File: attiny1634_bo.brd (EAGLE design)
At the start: 49.5 x 22.2 mm, 11 parts, among them J1 AVR_SPI_PRG_6NS, Y1 12MHz

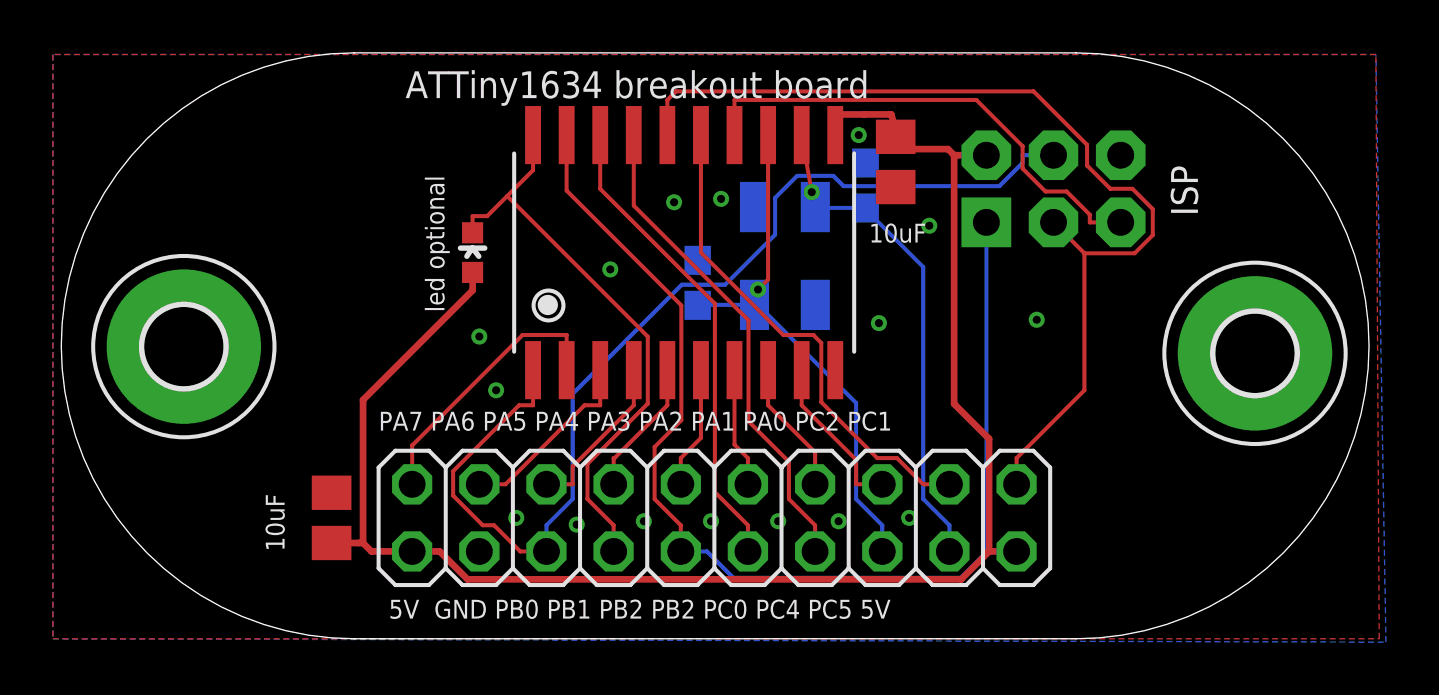
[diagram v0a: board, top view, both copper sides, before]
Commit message: small adjustment for better isolation
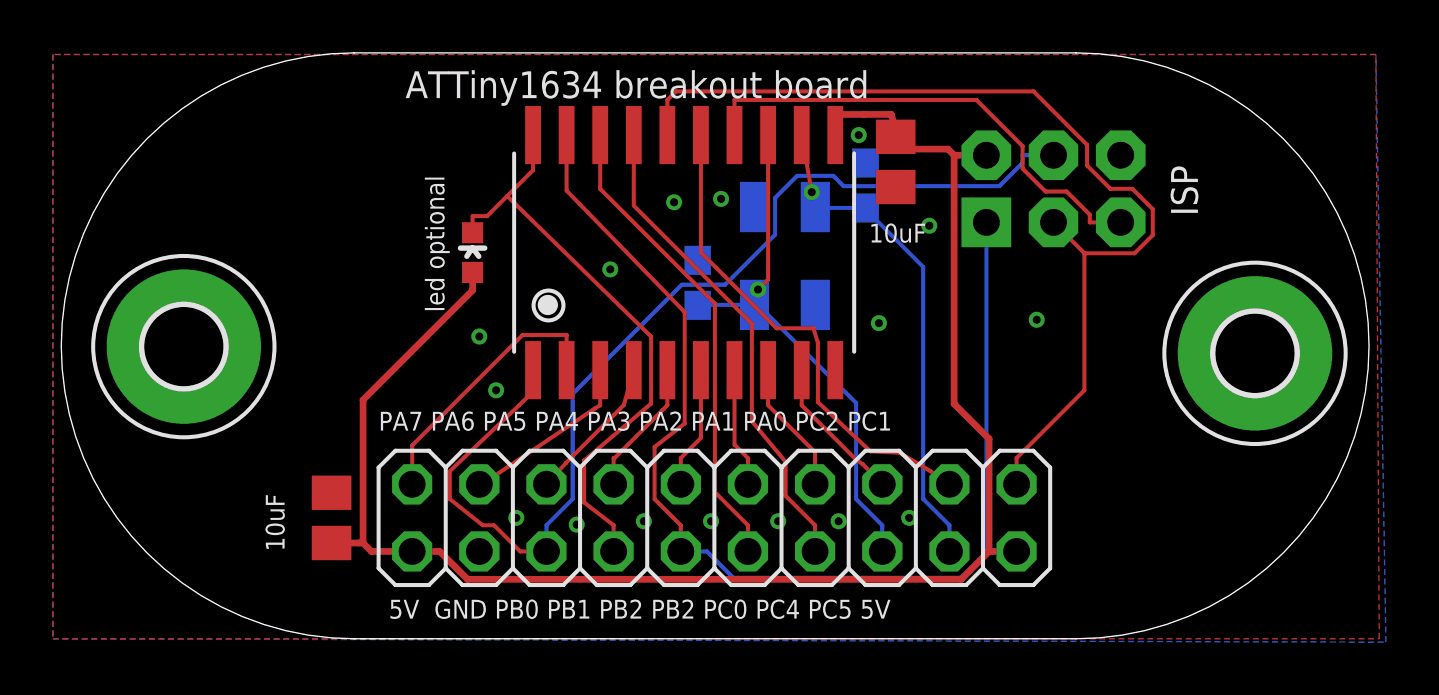
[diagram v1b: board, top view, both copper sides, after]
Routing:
- net PA5: track 6.27 -> 5.56 mm
- net PA0: track 6.16 -> 5.60 mm
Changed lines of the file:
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@@
 <wire x1="16.4234" y1="15.9837" x2="15.875" y2="15.9837" width="0.1524" layer="1"/>
 <wire x1="18.161" y1="17.7213" x2="17.1836" y2="16.7439" width="0.1524" layer="1"/>
-<wire x1="17.1836" y1="16.7439" x2="22.4998" y2="11.4277" width="0.1524" layer="1"/>
-<wire x1="22.4998" y1="11.4277" x2="22.4998" y2="8.8944" width="0.1524" layer="1"/>
-<wire x1="22.4998" y1="8.8944" x2="20.2183" y2="6.6129" width="0.1524" layer="1"/>
-<wire x1="20.2183" y1="6.6129" x2="20.2183" y2="5.2834" width="0.1524" layer="1"/>
-<wire x1="20.2183" y1="5.2834" x2="21.209" y2="4.2927" width="0.1524" layer="1"/>
+<wire x1="17.1836" y1="16.7439" x2="22.6268" y2="11.4277" width="0.1524" layer="1"/>
+<wire x1="22.6268" y1="11.4277" x2="22.6268" y2="8.8944" width="0.1524" layer="1"/>
+<wire x1="22.6268" y1="8.8944" x2="20.0913" y2="6.7399" width="0.1524" layer="1"/>
+<wire x1="20.0913" y1="6.7399" x2="20.0913" y2="5.1564" width="0.1524" layer="1"/>
+<wire x1="20.0913" y1="5.1564" x2="21.209" y2="4.2927" width="0.1524" layer="1"/>
 <wire x1="21.209" y1="3.302" x2="21.209" y2="4.2927" width="0.1524" layer="1"/>
 <wire x1="15.875" y1="15.355" x2="15.875" y2="15.9837" width="0.1524" layer="1"/>
@@
 <contactref element="JP1" pad="16"/>
 <wire x1="18.669" y1="3.302" x2="17.6783" y2="3.302" width="0.1524" layer="1"/>
-<wire x1="18.161" y1="10.16" x2="18.161" y2="8.8313" width="0.1524" layer="1"/>
-<wire x1="18.161" y1="8.8313" x2="17.6323" y2="8.8313" width="0.1524" layer="1"/>
-<wire x1="17.6323" y1="8.8313" x2="15.1382" y2="6.3372" width="0.1524" layer="1"/>
-<wire x1="15.1382" y1="6.3372" x2="15.1382" y2="5.4134" width="0.1524" layer="1"/>
-<wire x1="15.1382" y1="5.4134" x2="16.2589" y2="4.2927" width="0.1524" layer="1"/>
+<wire x1="18.161" y1="10.16" x2="18.161" y2="9.3393" width="0.1524" layer="1"/>
+<wire x1="18.161" y1="9.3393" x2="17.6323" y2="8.8313" width="0.1524" layer="1"/>
+<wire x1="17.6323" y1="8.8313" x2="15.0112" y2="6.3372" width="0.1524" layer="1"/>
+<wire x1="15.0112" y1="6.3372" x2="15.0112" y2="5.2864" width="0.1524" layer="1"/>
+<wire x1="15.0112" y1="5.2864" x2="16.2589" y2="4.2927" width="0.1524" layer="1"/>
 <wire x1="16.2589" y1="4.2927" x2="16.6876" y2="4.2927" width="0.1524" layer="1"/>
 <wire x1="16.6876" y1="4.2927" x2="17.6783" y2="3.302" width="0.1524" layer="1"/>
@@
 <wire x1="23.749" y1="3.302" x2="23.749" y2="4.2927" width="0.1524" layer="1"/>
 <wire x1="19.431" y1="19.05" x2="19.431" y2="16.9479" width="0.1524" layer="1"/>
-<wire x1="19.431" y1="16.9479" x2="23.7698" y2="12.6091" width="0.1524" layer="1"/>
-<wire x1="23.7698" y1="12.6091" x2="23.7698" y2="8.2657" width="0.1524" layer="1"/>
-<wire x1="23.7698" y1="8.2657" x2="22.7583" y2="7.2542" width="0.1524" layer="1"/>
+<wire x1="19.431" y1="16.9479" x2="23.8968" y2="12.3551" width="0.1524" layer="1"/>
+<wire x1="23.8968" y1="12.3551" x2="23.8968" y2="8.1387" width="0.1524" layer="1"/>
+<wire x1="23.8968" y1="8.1387" x2="22.7583" y2="7.2542" width="0.1524" layer="1"/>
 <wire x1="22.7583" y1="7.2542" x2="22.7583" y2="5.2834" width="0.1524" layer="1"/>
 <wire x1="22.7583" y1="5.2834" x2="23.749" y2="4.2927" width="0.1524" layer="1"/>
@@
 <contactref element="U$1" pad="9"/>
 <contactref element="JP1" pad="5"/>
-<wire x1="31.369" y1="5.842" x2="30.3783" y2="5.842" width="0.1524" layer="1"/>
+<wire x1="31.369" y1="5.842" x2="30.6323" y2="6.604" width="0.1524" layer="1"/>
 <wire x1="28.321" y1="10.16" x2="28.321" y2="8.8313" width="0.1524" layer="1"/>
 <wire x1="28.321" y1="8.8313" x2="30.3783" y2="6.774" width="0.1524" layer="1"/>
-<wire x1="30.3783" y1="6.774" x2="30.3783" y2="5.842" width="0.1524" layer="1"/>
+<wire x1="30.3783" y1="6.774" x2="30.6323" y2="6.604" width="0.1524" layer="1"/>
 </signal>
 <signal name="PA1">
@@
 <contactref element="JP1" pad="15"/>
 <contactref element="U$1" pad="4"/>
-<wire x1="18.669" y1="5.842" x2="19.6597" y2="5.842" width="0.1524" layer="1"/>
-<wire x1="21.971" y1="10.16" x2="21.971" y2="8.8313" width="0.1524" layer="1"/>
-<wire x1="21.971" y1="8.8313" x2="19.6597" y2="6.52" width="0.1524" layer="1"/>
-<wire x1="19.6597" y1="6.52" x2="19.6597" y2="5.842" width="0.1524" layer="1"/>
+<wire x1="18.669" y1="5.842" x2="18.8977" y2="6.096" width="0.1524" layer="1"/>
+<wire x1="21.971" y1="10.16" x2="21.59" y2="8.8313" width="0.1524" layer="1"/>
+<wire x1="21.59" y1="8.8313" x2="19.4057" y2="6.647" width="0.1524" layer="1"/>
+<wire x1="19.4057" y1="6.647" x2="18.8977" y2="6.096" width="0.1524" layer="1"/>
 </signal>
 <signal name="PA4">
@@
 <contactref element="JP1" pad="17"/>
 <contactref element="U$1" pad="3"/>
-<wire x1="16.129" y1="5.842" x2="17.1197" y2="5.842" width="0.1524" layer="1"/>
+<wire x1="16.129" y1="5.842" x2="16.6117" y2="6.096" width="0.1524" layer="1"/>
 <wire x1="20.701" y1="10.16" x2="20.701" y2="8.8313" width="0.1524" layer="1"/>
-<wire x1="20.701" y1="8.8313" x2="20.109" y2="8.8313" width="0.1524" layer="1"/>
-<wire x1="20.109" y1="8.8313" x2="17.1197" y2="5.842" width="0.1524" layer="1"/>
+<wire x1="20.701" y1="8.8313" x2="20.49" y2="8.7043" width="0.1524" layer="1"/>
+<wire x1="20.49" y1="8.7043" x2="16.6117" y2="6.096" width="0.1524" layer="1"/>
 </signal>
 <signal name="PB3/ADC8/OC1A">
@@
 <wire x1="28.829" y1="3.302" x2="28.829" y2="4.2927" width="0.1524" layer="1"/>
 <wire x1="21.971" y1="19.05" x2="21.971" y2="16.3787" width="0.1524" layer="1"/>
-<wire x1="21.971" y1="16.3787" x2="26.3098" y2="12.0399" width="0.1524" layer="1"/>
-<wire x1="26.3098" y1="12.0399" x2="26.3098" y2="8.2241" width="0.1524" layer="1"/>
-<wire x1="26.3098" y1="8.2241" x2="27.8383" y2="6.6956" width="0.1524" layer="1"/>
-<wire x1="27.8383" y1="6.6956" x2="27.8383" y2="5.2834" width="0.1524" layer="1"/>
-<wire x1="27.8383" y1="5.2834" x2="28.829" y2="4.2927" width="0.1524" layer="1"/>
+<wire x1="21.971" y1="16.3787" x2="26.4368" y2="11.9129" width="0.1524" layer="1"/>
+<wire x1="26.4368" y1="11.9129" x2="26.4368" y2="8.2241" width="0.1524" layer="1"/>
+<wire x1="26.4368" y1="8.2241" x2="27.7113" y2="6.6956" width="0.1524" layer="1"/>
+<wire x1="27.7113" y1="6.6956" x2="27.7113" y2="5.4104" width="0.1524" layer="1"/>
+<wire x1="27.7113" y1="5.4104" x2="28.829" y2="4.2927" width="0.1524" layer="1"/>
 </signal>
 <signal name="PC2/ADC11">
 <contactref element="U$1" pad="15"/>
 <contactref element="JP1" pad="3"/>
-<wire x1="33.909" y1="5.842" x2="32.9183" y2="5.842" width="0.1524" layer="1"/>
-<wire x1="32.9183" y1="5.842" x2="31.9276" y2="6.8327" width="0.1524" layer="1"/>
-<wire x1="31.9276" y1="6.8327" x2="31.1789" y2="6.8327" width="0.1524" layer="1"/>
-<wire x1="31.1789" y1="6.8327" x2="29.0622" y2="8.9494" width="0.1524" layer="1"/>
-<wire x1="29.0622" y1="8.9494" x2="29.0622" y2="11.1904" width="0.1524" layer="1"/>
-<wire x1="29.0622" y1="11.1904" x2="28.7638" y2="11.4888" width="0.1524" layer="1"/>
-<wire x1="28.7638" y1="11.4888" x2="27.6274" y2="11.4888" width="0.1524" layer="1"/>
-<wire x1="27.6274" y1="11.4888" x2="24.511" y2="14.6052" width="0.1524" layer="1"/>
+<wire x1="33.909" y1="5.842" x2="33.1723" y2="6.35" width="0.1524" layer="1"/>
+<wire x1="33.1723" y1="6.35" x2="32.0293" y2="7.0356" width="0.1524" layer="1"/>
+<wire x1="32.0293" y1="7.0356" x2="30.9249" y2="7.0867" width="0.1524" layer="1"/>
+<wire x1="30.9249" y1="7.0867" x2="28.9352" y2="8.9494" width="0.1524" layer="1"/>
+<wire x1="28.9352" y1="8.9494" x2="28.9352" y2="11.1904" width="0.1524" layer="1"/>
+<wire x1="28.9352" y1="11.1904" x2="28.7638" y2="11.7428" width="0.1524" layer="1"/>
+<wire x1="28.7638" y1="11.7428" x2="27.3734" y2="11.7428" width="0.1524" layer="1"/>
+<wire x1="27.3734" y1="11.7428" x2="24.511" y2="14.6052" width="0.1524" layer="1"/>
 <wire x1="24.511" y1="14.6052" x2="24.511" y2="19.05" width="0.1524" layer="1"/>
 </signal>

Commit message: I think it is now good enough
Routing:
- net PC1/SCL/ADC10: track 37.4 -> 38.1 mm
- net +5V: track 62.5 -> 63.2 mm
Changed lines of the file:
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@@
 <contactref element="U$1" pad="11"/>
 <wire x1="34.0867" y1="18.288" x2="34.0867" y2="8.8837" width="0.254" layer="1"/>
-<wire x1="34.0867" y1="8.8837" x2="35.4075" y2="7.5629" width="0.254" layer="1"/>
-<wire x1="35.4075" y1="7.5629" x2="35.4075" y2="3.302" width="0.254" layer="1"/>
+<wire x1="34.0867" y1="8.8837" x2="35.2805" y2="7.5629" width="0.254" layer="1"/>
+<wire x1="35.2805" y1="7.5629" x2="35.2805" y2="3.302" width="0.254" layer="1"/>
 <wire x1="34.1884" y1="18.288" x2="34.0867" y2="18.288" width="0.254" layer="1"/>
 <wire x1="35.306" y1="18.288" x2="34.1884" y2="18.288" width="0.254" layer="1"/>
@@
 <wire x1="11.5705" y1="3.622" x2="11.7305" y2="3.622" width="0.254" layer="1"/>
 <wire x1="15.875" y1="13.855" x2="15.875" y2="13.1755" width="0.254" layer="1"/>
-<wire x1="13.589" y1="3.302" x2="14.6305" y2="3.302" width="0.254" layer="1"/>
-<wire x1="36.449" y1="3.302" x2="35.4075" y2="3.302" width="0.254" layer="1"/>
-<wire x1="35.4075" y1="3.302" x2="34.3525" y2="2.247" width="0.254" layer="1"/>
-<wire x1="34.3525" y1="2.247" x2="15.6855" y2="2.247" width="0.254" layer="1"/>
-<wire x1="15.6855" y1="2.247" x2="14.6305" y2="3.302" width="0.254" layer="1"/>
+<wire x1="13.589" y1="3.302" x2="13.6145" y2="3.175" width="0.254" layer="1"/>
+<wire x1="36.449" y1="3.302" x2="35.2805" y2="3.302" width="0.254" layer="1"/>
+<wire x1="35.2805" y1="3.302" x2="34.7335" y2="1.993" width="0.254" layer="1"/>
+<wire x1="34.7335" y1="1.993" x2="14.6695" y2="1.866" width="0.254" layer="1"/>
+<wire x1="14.6695" y1="1.866" x2="13.6145" y2="3.175" width="0.254" layer="1"/>
 <wire x1="31.877" y1="18.5193" x2="33.8554" y2="18.5193" width="0.254" layer="1"/>
 <wire x1="33.8554" y1="18.5193" x2="34.0867" y2="18.288" width="0.254" layer="1"/>
@@
 <contactref element="JP1" pad="1"/>
 <wire x1="36.449" y1="5.842" x2="36.449" y2="6.8327" width="0.1524" layer="1"/>
-<wire x1="39.0146" y1="14.5794" x2="37.846" y2="15.748" width="0.1524" layer="1"/>
+<wire x1="39.0146" y1="14.4524" x2="37.846" y2="15.748" width="0.1524" layer="1"/>
 <wire x1="23.241" y1="20.3787" x2="23.5659" y2="20.7036" width="0.1524" layer="1"/>
 <wire x1="23.5659" y1="20.7036" x2="37.0917" y2="20.7036" width="0.1524" layer="1"/>
-<wire x1="37.0917" y1="20.7036" x2="39.116" y2="18.6793" width="0.1524" layer="1"/>
-<wire x1="39.116" y1="18.6793" x2="39.116" y2="17.8979" width="0.1524" layer="1"/>
-<wire x1="39.116" y1="17.8979" x2="39.9959" y2="17.018" width="0.1524" layer="1"/>
-<wire x1="39.9959" y1="17.018" x2="40.8315" y2="17.018" width="0.1524" layer="1"/>
-<wire x1="40.8315" y1="17.018" x2="41.6008" y2="16.2487" width="0.1524" layer="1"/>
-<wire x1="41.6008" y1="16.2487" x2="41.6008" y2="15.265" width="0.1524" layer="1"/>
-<wire x1="41.6008" y1="15.265" x2="40.9152" y2="14.5794" width="0.1524" layer="1"/>
-<wire x1="40.9152" y1="14.5794" x2="39.0146" y2="14.5794" width="0.1524" layer="1"/>
-<wire x1="39.0146" y1="14.5794" x2="39.0146" y2="9.3983" width="0.1524" layer="1"/>
+<wire x1="37.0917" y1="20.7036" x2="39.116" y2="19.0603" width="0.1524" layer="1"/>
+<wire x1="39.116" y1="19.0603" x2="39.116" y2="17.3899" width="0.1524" layer="1"/>
+<wire x1="39.116" y1="17.3899" x2="39.9959" y2="17.018" width="0.1524" layer="1"/>
+<wire x1="39.9959" y1="17.018" x2="41.2125" y2="17.018" width="0.1524" layer="1"/>
+<wire x1="41.2125" y1="17.018" x2="41.7278" y2="16.2487" width="0.1524" layer="1"/>
+<wire x1="41.7278" y1="16.2487" x2="41.7278" y2="15.265" width="0.1524" layer="1"/>
+<wire x1="41.7278" y1="15.265" x2="40.9152" y2="14.4524" width="0.1524" layer="1"/>
+<wire x1="40.9152" y1="14.4524" x2="39.0146" y2="14.4524" width="0.1524" layer="1"/>
+<wire x1="39.0146" y1="14.4524" x2="39.0146" y2="9.3983" width="0.1524" layer="1"/>
 <wire x1="39.0146" y1="9.3983" x2="36.449" y2="6.8327" width="0.1524" layer="1"/>
 <wire x1="23.241" y1="19.05" x2="23.241" y2="20.3787" width="0.1524" layer="1"/>
@@
 <contactref element="U$1" pad="14"/>
 <contactref element="J1" pad="5"/>
-<wire x1="40.386" y1="15.748" x2="39.2175" y2="15.748" width="0.1524" layer="1"/>
+<wire x1="40.386" y1="15.748" x2="39.9795" y2="16.129" width="0.1524" layer="1"/>
 <wire x1="25.781" y1="19.05" x2="25.781" y2="20.3787" width="0.1524" layer="1"/>
 <wire x1="25.781" y1="20.3787" x2="34.9277" y2="20.3787" width="0.1524" layer="1"/>
-<wire x1="34.9277" y1="20.3787" x2="36.6774" y2="18.629" width="0.1524" layer="1"/>
-<wire x1="36.6774" y1="18.629" x2="36.6774" y2="17.7809" width="0.1524" layer="1"/>
-<wire x1="36.6774" y1="17.7809" x2="37.5418" y2="16.9165" width="0.1524" layer="1"/>
-<wire x1="37.5418" y1="16.9165" x2="38.3412" y2="16.9165" width="0.1524" layer="1"/>
-<wire x1="38.3412" y1="16.9165" x2="39.2175" y2="16.0402" width="0.1524" layer="1"/>
-<wire x1="39.2175" y1="16.0402" x2="39.2175" y2="15.748" width="0.1524" layer="1"/>
+<wire x1="34.9277" y1="20.3787" x2="36.5504" y2="18.883" width="0.1524" layer="1"/>
+<wire x1="36.5504" y1="18.883" x2="36.5504" y2="17.7809" width="0.1524" layer="1"/>
+<wire x1="36.5504" y1="17.7809" x2="37.1608" y2="17.0435" width="0.1524" layer="1"/>
+<wire x1="37.1608" y1="17.0435" x2="38.3412" y2="17.0435" width="0.1524" layer="1"/>
+<wire x1="38.3412" y1="17.0435" x2="38.7095" y2="17.0562" width="0.1524" layer="1"/>
+<wire x1="38.7095" y1="17.0562" x2="39.9795" y2="16.129" width="0.1524" layer="1"/>
 </signal>
 <signal name="PC5/XTAL1">
@@
 <contactref element="U$1" pad="4"/>
 <wire x1="18.669" y1="5.842" x2="18.8977" y2="6.096" width="0.1524" layer="1"/>
-<wire x1="21.971" y1="10.16" x2="21.59" y2="8.8313" width="0.1524" layer="1"/>
-<wire x1="21.59" y1="8.8313" x2="19.4057" y2="6.647" width="0.1524" layer="1"/>
-<wire x1="19.4057" y1="6.647" x2="18.8977" y2="6.096" width="0.1524" layer="1"/>
+<wire x1="21.971" y1="10.16" x2="21.844" y2="8.9583" width="0.1524" layer="1"/>
+<wire x1="21.844" y1="8.9583" x2="18.8977" y2="6.266" width="0.1524" layer="1"/>
+<wire x1="18.8977" y1="6.266" x2="18.8977" y2="6.096" width="0.1524" layer="1"/>
 </signal>
 <signal name="PA4">
@@
 <contactref element="JP1" pad="19"/>
 <contactref element="U$1" pad="2"/>
-<wire x1="19.431" y1="10.16" x2="19.431" y2="11.4887" width="0.1524" layer="1"/>
-<wire x1="19.431" y1="11.4887" x2="17.766" y2="11.4887" width="0.1524" layer="1"/>
-<wire x1="17.766" y1="11.4887" x2="13.589" y2="7.3117" width="0.1524" layer="1"/>
-<wire x1="13.589" y1="7.3117" x2="13.589" y2="5.842" width="0.1524" layer="1"/>
+<wire x1="19.431" y1="10.16" x2="19.431" y2="11.7427" width="0.1524" layer="1"/>
+<wire x1="19.431" y1="11.7427" x2="17.766" y2="11.7427" width="0.1524" layer="1"/>
+<wire x1="17.766" y1="11.7427" x2="13.589" y2="7.4387" width="0.1524" layer="1"/>
+<wire x1="13.589" y1="7.4387" x2="13.589" y2="5.842" width="0.1524" layer="1"/>
 </signal>
 <signal name="PA6">
 <contactref element="JP1" pad="17"/>
 <contactref element="U$1" pad="3"/>
-<wire x1="16.129" y1="5.842" x2="16.6117" y2="6.096" width="0.1524" layer="1"/>
-<wire x1="20.701" y1="10.16" x2="20.701" y2="8.8313" width="0.1524" layer="1"/>
-<wire x1="20.701" y1="8.8313" x2="20.49" y2="8.7043" width="0.1524" layer="1"/>
-<wire x1="20.49" y1="8.7043" x2="16.6117" y2="6.096" width="0.1524" layer="1"/>
+<wire x1="16.129" y1="5.842" x2="16.4847" y2="6.477" width="0.1524" layer="1"/>
+<wire x1="20.701" y1="10.16" x2="20.574" y2="8.9487" width="0.1524" layer="1"/>
+<wire x1="20.574" y1="8.9487" x2="18.331" y2="8.3233" width="0.1524" layer="1"/>
+<wire x1="18.331" y1="8.3233" x2="16.4847" y2="6.477" width="0.1524" layer="1"/>
 </signal>
 <signal name="PB3/ADC8/OC1A">
